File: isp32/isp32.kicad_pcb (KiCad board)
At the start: 2 copper layers, 55.5 x 48.5 mm, 99 parts, among them J1 BAT1, J2 Switching, J3 USB_C_Receptacle_USB2.0, J4 ESP_JTAG, J5 GPS_ANT, J6 F0, J7 F1, J8 Flash_SPI, M1 Motor_Servo, M2 Motor_Servo, M3 Motor_Servo, M4 Motor_Servo, Q1 BSS138, Q2 BSS138, Q3 IRLML6402, Q4 BSS138, Q5 IRLML6402, Q6 S8050, Q7 S8050, Q8 S8050, SW1 RST, SW2 IO0, U10 BMP280, U11 MPU-9250, U12 CH340C, U2 USBLC6-2SC6, U3 ESP32-WROOM-32U, U4 AMS1117-3.3, U5 MP2303ADN, U7 NEO-XM, U8 AT25SF081-SSHD-X, U9 RFM98W-315S2

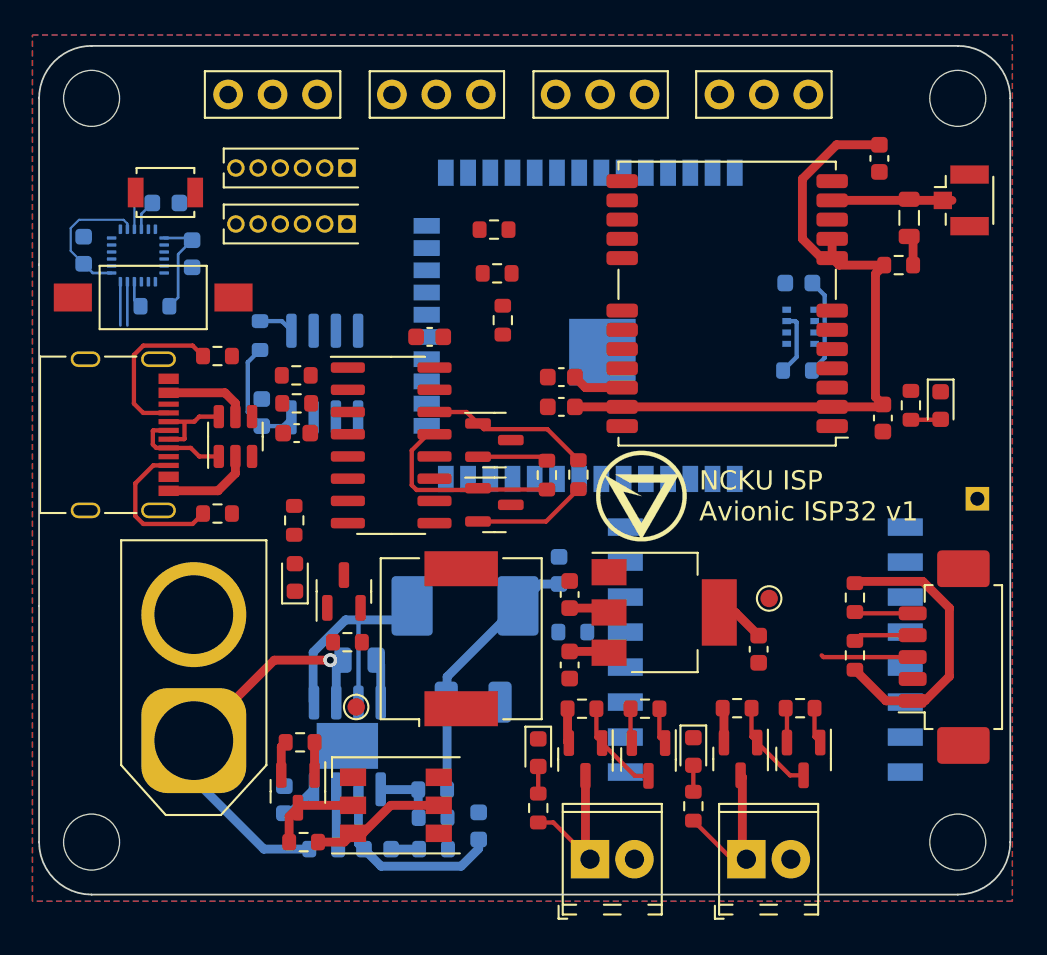
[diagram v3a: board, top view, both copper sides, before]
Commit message: Add M3 mounting hole
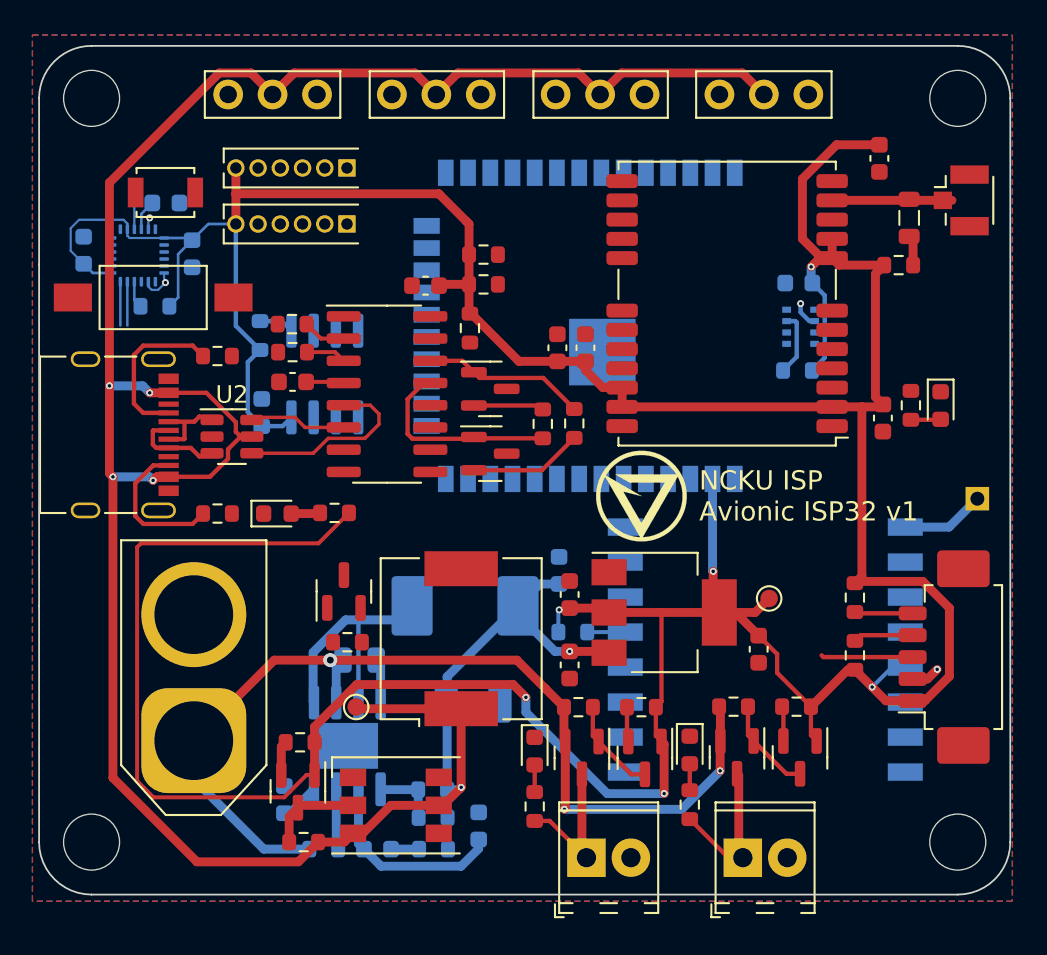
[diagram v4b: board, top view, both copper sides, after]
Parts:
- removed REF** (x4): MountingHole_3.2mm_M3_DIN965, MountingHole:MountingHole_3.2mm_M3_DIN965
- added H1: MountingHole, MountingHole:MountingHole_3.2mm_M3_ISO7380, F.Cu at (62.6, 40.8)
- added H2: MountingHole, MountingHole:MountingHole_3.2mm_M3_ISO7380, F.Cu at (62.6, 83.3)
- added H3: MountingHole, MountingHole:MountingHole_3.2mm_M3_ISO7380, F.Cu at (112.1, 83.3)
- added H4: MountingHole, MountingHole:MountingHole_3.2mm_M3_ISO7380, F.Cu at (112.1, 40.8)
- moved D5 3.78 mm to (73.2, 64.5), turned to 0 degrees
- moved C13 3.38 mm to (89.2, 55.0), turned to 90 degrees
- moved C25 2.94 mm to (81.7, 51.5)
- moved C26 2.94 mm to (74.1, 57.0)
- moved R26 2.94 mm to (74.0, 53.7)
- moved R27 2.94 mm to (74.1, 55.3)
- moved R29 2.94 mm to (90.2, 59.3)
- moved U12 2.94 mm to (79.5, 57.7)
- moved Q8 2.94 mm to (85.4, 61.1)
- moved Q7 2.94 mm to (85.4, 57.4)
- moved R28 2.94 mm to (88.4, 59.4)
- moved R18 2.34 mm to (76.5, 64.5), turned to 180 degrees
- moved C11 2.17 mm to (90.8, 55.0), turned to 90 degrees
- moved R1 1.93 mm to (84.2, 53.9)
- moved R2 1.55 mm to (85.0, 49.7)
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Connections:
- U2 pad 1: Net-(J3-PadA6) -> Net-(J3-PadA7)
- U2 pad 3: D+ -> Net-(J3-PadA6)
- U2 pad 4: D- -> D+
- U2 pad 6: Net-(J3-PadA7) -> D-
- U3 pad 4: unconnected-(U3-Pad4) -> EXT_INT
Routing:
- net +3V3: track 99.5 -> 256.7 mm, vias 0 -> 6
- net +5V: track 29.9 -> 152.7 mm, vias 0 -> 6
- net +BATT: track 27.5 -> 57.3 mm, vias 1 -> 3
- net D+: track 0.00 -> 10.8 mm
- net D-: track 0.00 -> 5.55 mm
- net Net-(AE1-Pad1): track 0.00 -> 4.79 mm
- net Net-(R26-Pad2): track 0.00 -> 2.47 mm
- net Net-(R27-Pad2): track 0.00 -> 2.31 mm
- net Net-(C26-Pad1): track 0.00 -> 2.18 mm
- net LORA_SS: track 0.00 -> 2.18 mm
- net Net-(D5-Pad2): track 0.00 -> 1.67 mm
- net GND: track 7.72 -> 8.42 mm, vias 0 -> 4

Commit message: Fix overlap
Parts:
- moved J1 0.88 mm to (67.8, 78.1)
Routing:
- net +3V3: track 256.7 -> 259.7 mm
- net +5V: track 152.7 -> 154.6 mm
- net +BATT: track 57.3 -> 57.9 mm

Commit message: Resolve overlap
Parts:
- moved J1 0.70 mm to (67.8, 77.4)
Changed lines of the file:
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@@
   )
   (footprint "Connector_AMASS:AMASS_XT60-M_1x02_P7.20mm_Vertical" (layer "F.Cu")
-    (at 67.8 78.1 90)
+    (at 67.8 77.4 90)
     (descr "AMASS female XT60, through hole, vertical, https://www.tme.eu/Document/2d152ced3b7a446066e6c419d84bb460/XT60%20SPEC.pdf")
     (tags "XT60 female vertical")
@@
   (segment (start 98.514 77.495) (end 98.514 75.6075) (width 0.508) (layer "F.Cu") (net 3))
   (segment (start 89.575 77.45) (end 89.65 77.525) (width 0.508) (layer "F.Cu") (net 3))
+  (segment (start 89.575 75.5625) (end 89.575 77.45) (width 0.508) (layer "F.Cu") (net 3))
   (segment (start 76.22068 72.87382) (end 73.02068 72.87382) (width 0.508) (layer "F.Cu") (net 3))
-  (segment (start 89.575 75.5625) (end 89.575 77.45) (width 0.508) (layer "F.Cu") (net 3))
-  (segment (start 73.02068 72.87382) (end 67.8 78.0945) (width 0.508) (layer "F.Cu") (net 3))
   (segment (start 86.88632 72.87382) (end 76.22068 72.87382) (width 0.508) (layer "F.Cu") (net 3))
   (segment (start 89.65 77.525) (end 89.65 81.35) (width 0.508) (layer "F.Cu") (net 3))
   (segment (start 89.65 81.35) (end 89.6 81.4) (width 0.508) (layer "F.Cu") (net 3))
-  (segment (start 67.8 78.0945) (end 67.8 78.1) (width 0.508) (layer "F.Cu") (net 3))
   (segment (start 98.514 75.6075) (end 98.439 75.5325) (width 0.508) (layer "F.Cu") (net 3))
+  (segment (start 73.02068 72.87382) (end 68.4945 77.4) (width 0.508) (layer "F.Cu") (net 3))
+  (segment (start 68.4945 77.4) (end 67.8 77.4) (width 0.508) (layer "F.Cu") (net 3))
   (segment (start 89.575 75.5625) (end 88.50625 74.49375) (width 0.508) (layer "F.Cu") (net 3))
   (via (at 98.5 79.2) (size 0.4) (drill 0.2) (layers "F.Cu" "B.Cu") (net 3))
   (via (at 89.6 81.4) (size 0.4) (drill 0.2) (layers "F.Cu" "B.Cu") (net 3))
   (via (at 76.22068 72.87382) (size 0.8) (drill 0.4) (layers "F.Cu" "B.Cu") (net 3))
-  (segment (start 67.8 79.05314) (end 72.42068 83.67382) (width 0.508) (layer "B.Cu") (net 3))
   (segment (start 76.56068 75.29382) (end 76.56068 73.25882) (width 0.508) (layer "B.Cu") (net 3))
   (segment (start 76.94568 72.87382) (end 76.22068 72.87382) (width 0.508) (layer "B.Cu") (net 3))
+  (segment (start 89.6 81.4) (end 96.3 81.4) (width 0.508) (layer "B.Cu") (net 3))
+  (segment (start 76.56068 73.25882) (end 76.94568 72.87382) (width 0.508) (layer "B.Cu") (net 3))
   (segment (start 72.42068 83.67382) (end 75.02068 83.67382) (width 0.508) (layer "B.Cu") (net 3))
-  (segment (start 89.6 81.4) (end 96.3 81.4) (width 0.508) (layer "B.Cu") (net 3))
-  (segment (start 67.8 78.1) (end 67.8 79.05314) (width 0.508) (layer "B.Cu") (net 3))
-  (segment (start 76.56068 73.25882) (end 76.94568 72.87382) (width 0.508) (layer "B.Cu") (net 3))
   (segment (start 96.3 81.4) (end 98.5 79.2) (width 0.508) (layer "B.Cu") (net 3))
+  (segment (start 67.8 79.05314) (end 72.42068 83.67382) (width 0.508) (layer "B.Cu") (net 3))
+  (segment (start 67.8 77.4) (end 67.8 79.05314) (width 0.508) (layer "B.Cu") (net 3))
   (segment (start 109.5 75.2) (end 107.975 75.2) (width 0.508) (layer "F.Cu") (net 4))
   (segment (start 95.3 80.5) (end 95.3 77.675) (width 0.508) (layer "F.Cu") (net 4))
@@
   (group "" (id cdbc1cd6-d87c-44c3-b9a7-f2f37c30c6e9)
     (members
-      06a55f37-4a17-4d25-b46f-63b1b529331c
       09f27e4a-3c7c-4198-be81-64ae03d1556b
       0af038ac-c246-4898-aa9f-d12759ac9141
@@
       2d391309-58f9-4f68-b19d-fbf9d476750c
       2f2afae1-2e54-41f2-98ec-6e9c9eb99e80
-      2fe244da-e2ef-4574-b20e-fea78530d8cf
       3131c7f7-4abe-4ca3-8525-32a17b59cc98
       3744d983-4ba5-4c15-9fff-3310c640b8ed
       376428f7-84b7-40da-8f8c-f5694b35a9fa
       465c5fc5-150e-4a6e-9fea-fc74eb481b27
-      493baf2c-70a0-4313-b032-ebb6bdfbae1c
       59806e5d-da1d-4251-8231-14f70028a482
       62132788-bf25-4459-a35d-faff718df276
       65d4c3b9-0f1e-4df3-916e-bb2c8494cac4
       662be10b-867e-4dff-a2ea-68903e21f757
-      68d2f487-2fd7-490c-b647-3bd0dda9888f
+      6a52fb81-a204-4f86-a3f2-202aa553c12a
       6cf48b32-5813-4ebd-bb21-461242ff6d36
       7089bd85-01c2-4079-90d0-cc99c590c4a7
@@
       740b4c2f-854b-4332-a519-4069ab745986
       746266a9-5a39-4118-8753-585641cd0ec5
-      7ac4b5a4-eef1-4aa4-9c57-271af75cd46a
       81c6df9f-3bad-4452-a254-aa9fbe3712f6
       8416199d-d161-4b90-a9a2-11fdbdcf4099
       87644e4e-0b8a-400a-b756-2ddf5904fb49
+      8c7705f8-a837-4a7c-8617-c9f4cbf408ed
       96d4be42-4937-4a3d-83ea-29a7ffae9673
       976e6119-24bf-4c29-a13d-80b14b49079c
       98cb5a8b-b201-4f39-8e16-022bf7e98f80
+      9919065d-54e0-4e66-bdab-27cddee8308c
       9936828e-5a02-4875-8aad-114cc4719c85
       a1fbc6bd-ec6a-492a-87bc-8f17d30bcd11
       a887255b-c877-4c6c-ae3a-c946821a9bdf
-      af51309f-0c7d-4976-96b8-4ce1e5f2451d
       b0aef279-4e9c-45c6-a165-3214fb46a170
+      b691342b-f21c-4912-85f4-fb242cb6aefd
       b96a0aa7-b143-4b2b-8758-dee2606e6306
       c7047929-8800-433f-a7c9-4fc4898d9dcc
@@
       d58f1c07-e3df-4037-a984-e12cf2390921
       d7d51dc5-4651-4e5f-bc07-c174d48abdda
+      d84adbf5-0a3a-438d-bd96-27a8ccc4e409
       da76c8f7-6a11-4673-836e-cc37d0257f35
       db1adcf1-d60c-4d1a-9cb7-a7ac1fd0b039
+      dd8745d0-d237-4b9a-ba86-4bbe8bd0adc6
       de4c9fc0-d579-4928-b342-12f8d3978f8d
       e11a4f1b-8698-4ffd-81c9-98612048aece

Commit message: Complete routing
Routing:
- net MOSI: track 2.50 -> 99.6 mm
- net MISO: track 2.10 -> 92.2 mm
- net IO0: track 1.97 -> 91.8 mm, vias 0 -> 2
- net SCK: track 2.50 -> 87.8 mm, vias 0 -> 1
- net SDA: track 3.33 -> 56.4 mm, vias 0 -> 2
- net SCL: track 3.43 -> 52.0 mm, vias 0 -> 2
- net RXD: track 0.00 -> 45.8 mm, vias 0 -> 1
- net Net-(R13-Pad1): track 0.00 -> 41.7 mm
- net GND: track 8.42 -> 50.1 mm, vias 4 -> 31
- net TXD: track 0.00 -> 41.2 mm, vias 0 -> 1
- net RST: track 0.00 -> 36.0 mm, vias 0 -> 1
- net IMU_SS: track 1.54 -> 30.1 mm, vias 0 -> 2
- net TMS: track 0.00 -> 25.9 mm
- net SERVO0: track 0.00 -> 25.5 mm, vias 0 -> 1
- net TDI: track 0.00 -> 24.2 mm
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
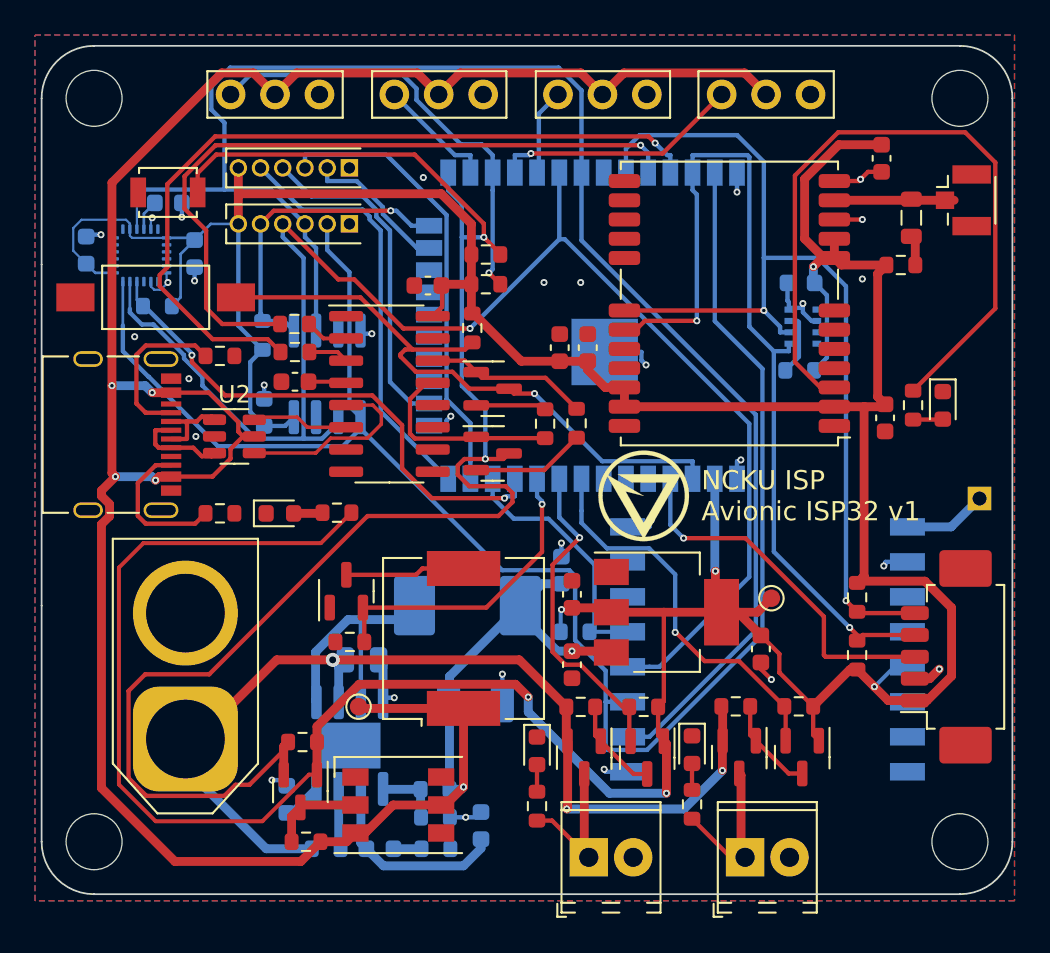
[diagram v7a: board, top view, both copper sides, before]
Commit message: Add vias
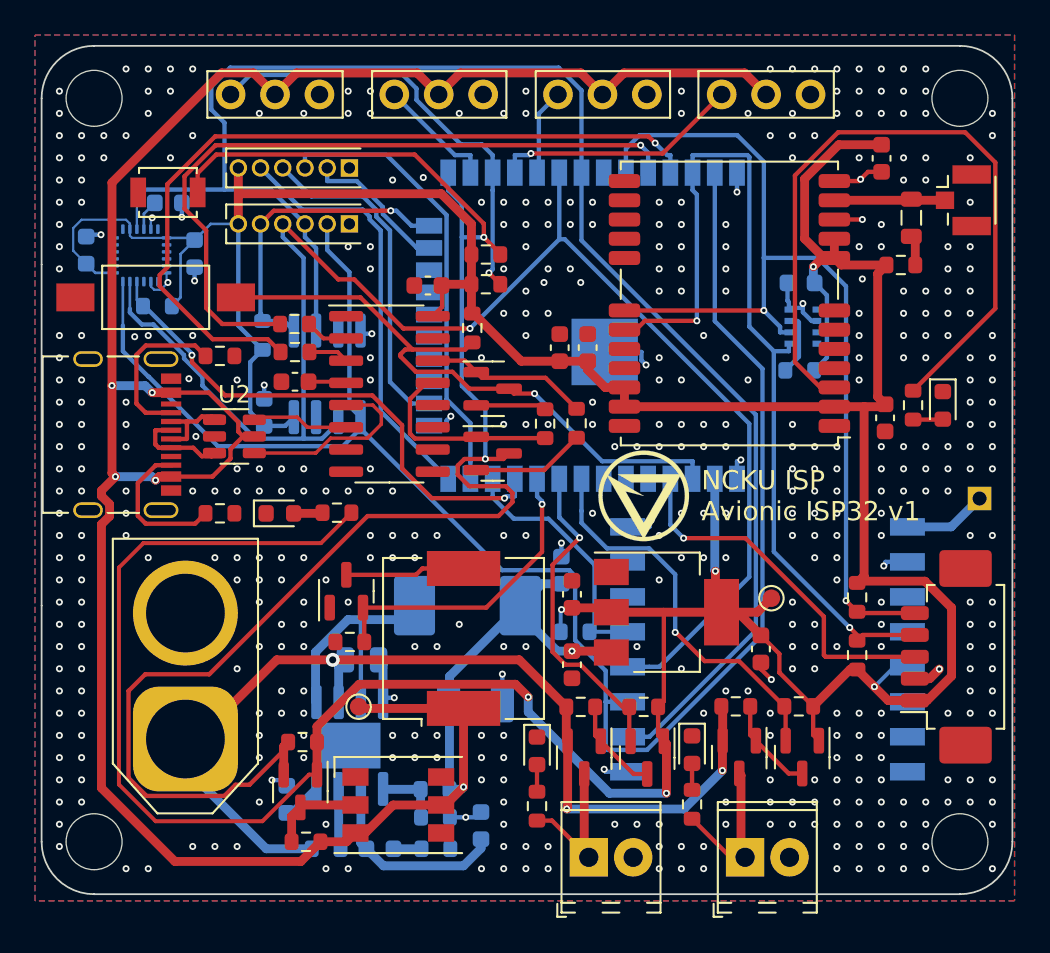
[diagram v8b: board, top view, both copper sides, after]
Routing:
- net +3V3: track 261.7 -> 260.9 mm
- net Net-(J5-Pad1): track 6.94 -> 6.41 mm
- net GND: vias 31 -> 474
